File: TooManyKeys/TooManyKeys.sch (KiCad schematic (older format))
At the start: 60 parts, among them J1 54104-3031_Oled, J2 AVR-ISP-6(SWR204-NRTN-D03-RA-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, SW1 SW_Push, U1 PRTR5V0U2X, U2 AT90USB1286-AU, U3 PCA9306, U4 AZ1117CH-3.3TRG1, Y1 16MHz

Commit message: New footprint, pcb key matrix completed
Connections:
- net COL18 is gone; now on net COL14: U2.2 (PE7)
- net ROW2 is gone; now on net ROW1: U2.49 (PA2)
- net COL08: now also U2.58 (PF3); no longer U2.27 (PD2)
- net COL09: now also U2.59 (PF2); no longer U2.28 (PD3)
- net COL10: now also U2.60 (PF1); no longer U2.29 (PD4)
- net COL11: now also U2.61 (PF0); no longer U2.30 (PD5)
- net COL12: now also U2.33 (PE0); no longer U2.31 (PD6)
- net COL13: now also U2.34 (PE1); no longer U2.32 (PD7)
- net COL14: no longer U2.9 (PE3)
- net COL15: now also U2.32 (PD7); no longer U2.18 (PE4)
- net COL16: now also U2.31 (PD6); no longer U2.19 (PE5)
- net COL19: now also U2.57 (PF4); no longer U2.61 (PF0)
- net COL20: now also U2.56 (PF5); no longer U2.60 (PF1)
- net COL21: now also U2.55 (PF6); no longer U2.59 (PF2)
- net COL22: now also U2.54 (PF7); no longer U2.58 (PF3)
- net ROW0: now also U2.50 (PA1); no longer U2.51 (PA0)
- net ROW1: no longer U2.50 (PA1)
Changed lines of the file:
@@
 Text GLabel 9050 1500 2    50   Input ~ 0
 D-
-$Sheet
-S 1850 6650 1100 550
-U 5E8A6E89
-F0 "Matrix" 50
-F1 "Matrix.sch" 50
-$EndSheet
 $Comp
 L TooManyKeys-rescue:HRO-TYPE-C-31-M-12-Type-C USB1
@@
 Text GLabel 3700 4000 2    50   Input ~ 0
 SDA
-Text GLabel 3700 1300 2    50   Input ~ 0
+Text GLabel 3700 1400 2    50   Input ~ 0
 ROW1
-Text GLabel 3700 1400 2    50   Input ~ 0
-ROW2
 Text GLabel 3700 1500 2    50   Input ~ 0
 ROW3
@@
 Text GLabel 3700 1900 2    50   Input ~ 0
 ROW7
-Text GLabel 3700 1200 2    50   Input ~ 0
+Text GLabel 3700 1300 2    50   Input ~ 0
 ROW0
 Text GLabel 3700 3000 2    50   Input ~ 0
@@
 Text GLabel 3700 3700 2    50   Input ~ 0
 COL07
-Text GLabel 3700 4100 2    50   Input ~ 0
+Text GLabel 2300 4200 0    50   Input ~ 0
 COL08
-Text GLabel 3700 4200 2    50   Input ~ 0
+Text GLabel 2300 4100 0    50   Input ~ 0
 COL09
-Text GLabel 3700 4300 2    50   Input ~ 0
+Text GLabel 2300 4000 0    50   Input ~ 0
 COL10
-Text GLabel 3700 4400 2    50   Input ~ 0
+Text GLabel 2300 3900 0    50   Input ~ 0
 COL11
+Text GLabel 2250 3000 0    50   Input ~ 0
+COL12
+Text GLabel 2250 3100 0    50   Input ~ 0
+COL13
+Text GLabel 2250 3700 0    50   Input ~ 0
+COL14
+Text GLabel 3700 4600 2    50   Input ~ 0
+COL15
 Text GLabel 3700 4500 2    50   Input ~ 0
-COL12
-Text GLabel 3700 4600 2    50   Input ~ 0
-COL13
-Text GLabel 2250 3300 0    50   Input ~ 0
-COL14
-Text GLabel 2250 3400 0    50   Input ~ 0
-COL15
-Text GLabel 2250 3500 0    50   Input ~ 0
 COL16
 Text GLabel 2250 3600 0    50   Input ~ 0
 COL17
-Text GLabel 2250 3700 0    50   Input ~ 0
-COL18
-Text GLabel 2250 3900 0    50   Input ~ 0
+Text GLabel 2250 4300 0    50   Input ~ 0
 COL19
-Text GLabel 2250 4000 0    50   Input ~ 0
+Text GLabel 2250 4400 0    50   Input ~ 0
 COL20
-Text GLabel 2250 4100 0    50   Input ~ 0
+Text GLabel 2250 4500 0    50   Input ~ 0
 COL21
-Text GLabel 2250 4200 0    50   Input ~ 0
+Text GLabel 2250 4600 0    50   Input ~ 0
 COL22
-$Sheet
-S 3050 6650 1000 550
-U 6065500F
-F0 "Led" 50
-F1 "Led.sch" 50
-$EndSheet
 Wire Wire Line
 	10800 1750 12050 1750
@@
 Text GLabel 15550 6400 2    50   Input ~ 0
 CS28
-$Comp
-L TooManyKeys-rescue:505110-3091_Oled-SamacSys_Parts J1
-U 1 1 604722A8
-P 13050 1050
-F 0 "J1" H 13550 1315 50  0000 C CNN
-F 1 "54104-3031_Oled" H 13550 1224 50  0000 C CNN
-F 2 "SamacSys_Parts:0541043033" H 13900 1150 50  0001 L CNN
-F 3 "https://componentsearchengine.com/Datasheets/1/505110-3091.pdf" H 13900 1050 50  0001 L CNN
-F 4 "MOLEX - 505110-3091 - CONNECTOR, FFC/FPC, 30POS, 1ROW, 0.5MM" H 13900 950 50  0001 L CNN "Description"
-F 5 "2.1" H 13900 850 50  0001 L CNN "Height"
-F 6 "538-505110-3091" H 13900 750 50  0001 L CNN "Mouser Part Number"
-F 7 "https://www.mouser.com/Search/Refine.aspx?Keyword=538-505110-3091" H 13900 650 50  0001 L CNN "Mouser Price/Stock"
-F 8 "Molex" H 13900 550 50  0001 L CNN "Manufacturer_Name"
-F 9 "505110-3091" H 13900 450 50  0001 L CNN "Manufacturer_Part_Number"
-	1    13050 1050
-	-1   0    0    -1
-$EndComp
 Text GLabel 11300 6850 2    50   Input ~ 0
 CS1
@@
 	3600 4000 3700 4000
 Wire Wire Line
-	3700 4100 3600 4100
-Wire Wire Line
-	3700 4200 3600 4200
-Wire Wire Line
-	3700 4300 3600 4300
-Wire Wire Line
-	3700 4400 3600 4400
+	2300 4200 2400 4200
+Wire Wire Line
+	2300 4100 2400 4100
+Wire Wire Line
+	2300 4000 2400 4000
+Wire Wire Line
+	2300 3900 2400 3900
 Wire Wire Line
 	3600 4500 3700 4500
@@
 	3700 4600 3600 4600
 Wire Wire Line
-	2250 3300 2400 3300
-Wire Wire Line
-	2250 3400 2400 3400
-Wire Wire Line
-	2250 3500 2400 3500
+	2250 3700 2400 3700
+Wire Wire Line
+	2250 3000 2400 3000
+Wire Wire Line
+	2250 3100 2400 3100
 Wire Wire Line
 	2250 3600 2400 3600
 Wire Wire Line
-	2250 3700 2400 3700
-Wire Wire Line
-	2250 3900 2400 3900
-Wire Wire Line
-	2250 4000 2400 4000
-Wire Wire Line
-	2250 4100 2400 4100
-Wire Wire Line
-	2250 4200 2400 4200
+	2250 4300 2400 4300
+Wire Wire Line
+	2250 4400 2400 4400
+Wire Wire Line
+	2250 4500 2400 4500
+Wire Wire Line
+	2250 4600 2400 4600
 Wire Wire Line
 	2400 2200 2150 2200
@@
 Text Label 3900 2200 2    50   ~ 0
 SCK
-Wire Wire Line
-	3700 1200 3600 1200
 Wire Wire Line
 	3700 1300 3600 1300
@@
 	1700 1200 2050 1200
 Connection ~ 2050 1200
+$Comp
+L TooManyKeys-rescue:505110-3091_Oled-SamacSys_Parts J1
+U 1 1 604722A8
+P 13050 1050
+F 0 "J1" H 13550 1315 50  0000 C CNN
+F 1 "54104-3031_Oled" H 13550 1224 50  0000 C CNN
+F 2 "SamacSys_Parts:0541043033" H 13900 1150 50  0001 L CNN
+F 3 "https://componentsearchengine.com/Datasheets/1/505110-3091.pdf" H 13900 1050 50  0001 L CNN
+F 4 "MOLEX - 505110-3091 - CONNECTOR, FFC/FPC, 30POS, 1ROW, 0.5MM" H 13900 950 50  0001 L CNN "Description"
+F 5 "2.1" H 13900 850 50  0001 L CNN "Height"
+F 6 "538-505110-3091" H 13900 750 50  0001 L CNN "Mouser Part Number"
+F 7 "https://www.mouser.com/Search/Refine.aspx?Keyword=538-505110-3091" H 13900 650 50  0001 L CNN "Mouser Price/Stock"
+F 8 "Molex" H 13900 550 50  0001 L CNN "Manufacturer_Name"
+F 9 "505110-3091" H 13900 450 50  0001 L CNN "Manufacturer_Part_Number"
+	1    13050 1050
+	-1   0    0    -1
+$EndComp
+$Sheet
+S 3050 6650 1000 550
+U 6065500F
+F0 "Led" 50
+F1 "Led.sch" 50
+$EndSheet
+$Sheet
+S 1850 6650 1100 550
+U 5E8A6E89
+F0 "Matrix" 50
+F1 "Matrix.sch" 50
+$EndSheet
 $EndSCHEMATC

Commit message: New led symbols and footprint
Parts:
- J2: value AVR-ISP-6(SWR204-NRTN-D03-RA-GA) -> AVR-ISP-6
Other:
- note added: "30 Pins Oled Connector"
- note added: "Connector Header\nRight Angle 6 position 2.00mm"
- note added: "Crystal"
- note added: "Dual bidirectional I2C-bus and SMBus voltage-level translator"
- note added: "Fuse"
- note added: "Low Dropout Regulators"
- note added: "MCU"
- note added: "MCU Decoplings"
- note added: "Master Led Driver"
- note added: "Salve Led Driver"
- note added: "USB Type-C"
- moved on the sheet: C1, C10, C11, C12, C13, C14, C15, C16, C17, C18, C19, C2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

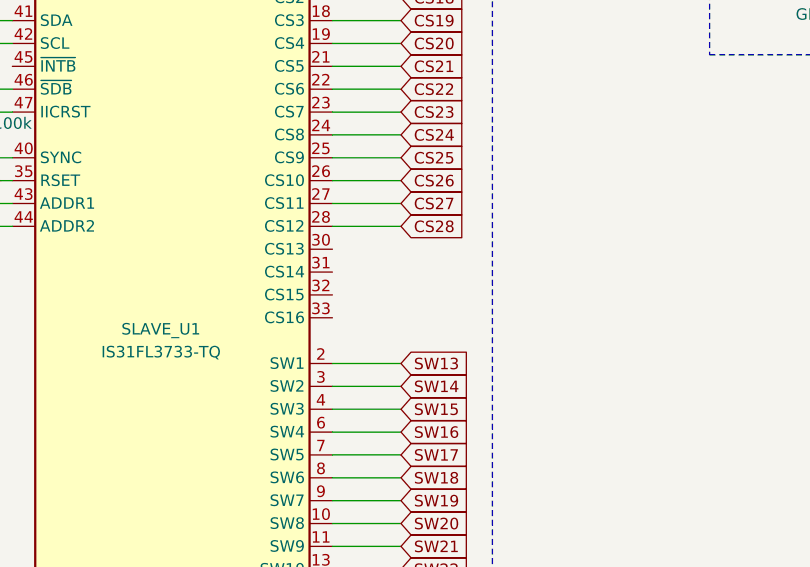
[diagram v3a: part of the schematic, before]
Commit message: RBG Led replaced
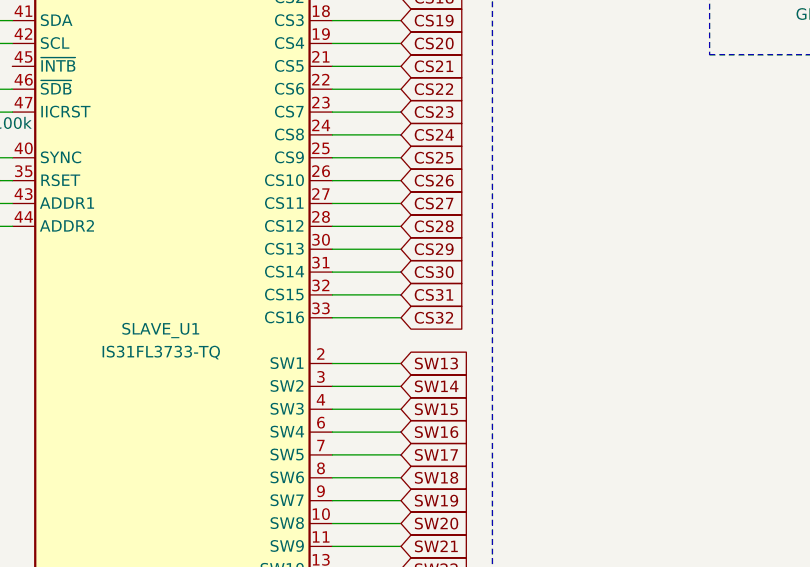
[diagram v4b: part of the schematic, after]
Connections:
- net CS29: now reaches SLAVE_U1.30 (CS13)
- net CS30: now reaches SLAVE_U1.31 (CS14)
- net CS31: now reaches SLAVE_U1.32 (CS15)
- net CS32: now reaches SLAVE_U1.33 (CS16)
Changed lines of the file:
@@
 Wire Notes Line
 	4600 600  1500 600
+Text GLabel 11700 7800 2    50   Input ~ 0
+CS29
+Text GLabel 11700 7900 2    50   Input ~ 0
+CS30
+Text GLabel 11700 8000 2    50   Input ~ 0
+CS31
+Text GLabel 11700 8100 2    50   Input ~ 0
+CS32
+Wire Wire Line
+	11400 7800 11700 7800
+Wire Wire Line
+	11700 7900 11400 7900
+Wire Wire Line
+	11400 8000 11700 8000
+Wire Wire Line
+	11700 8100 11400 8100
 $EndSCHEMATC
